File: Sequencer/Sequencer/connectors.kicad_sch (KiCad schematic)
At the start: 1 part, among them J13 Conn_02x05_Odd_Even

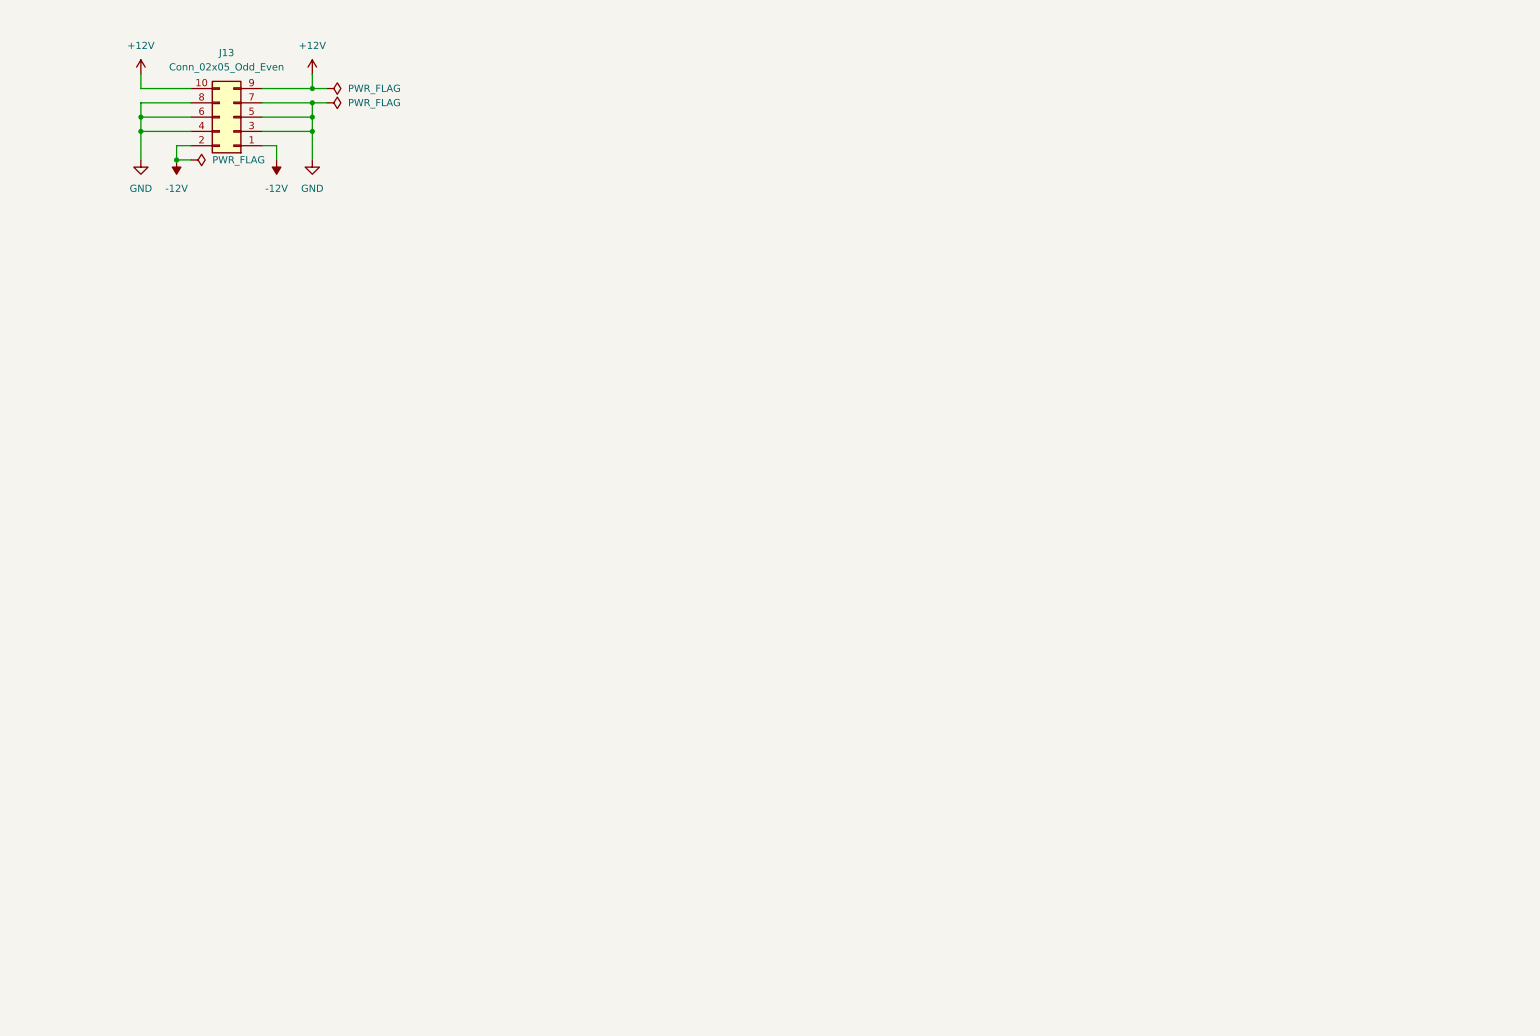
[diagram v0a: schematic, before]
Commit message: Sequencer - schematic mostly complete
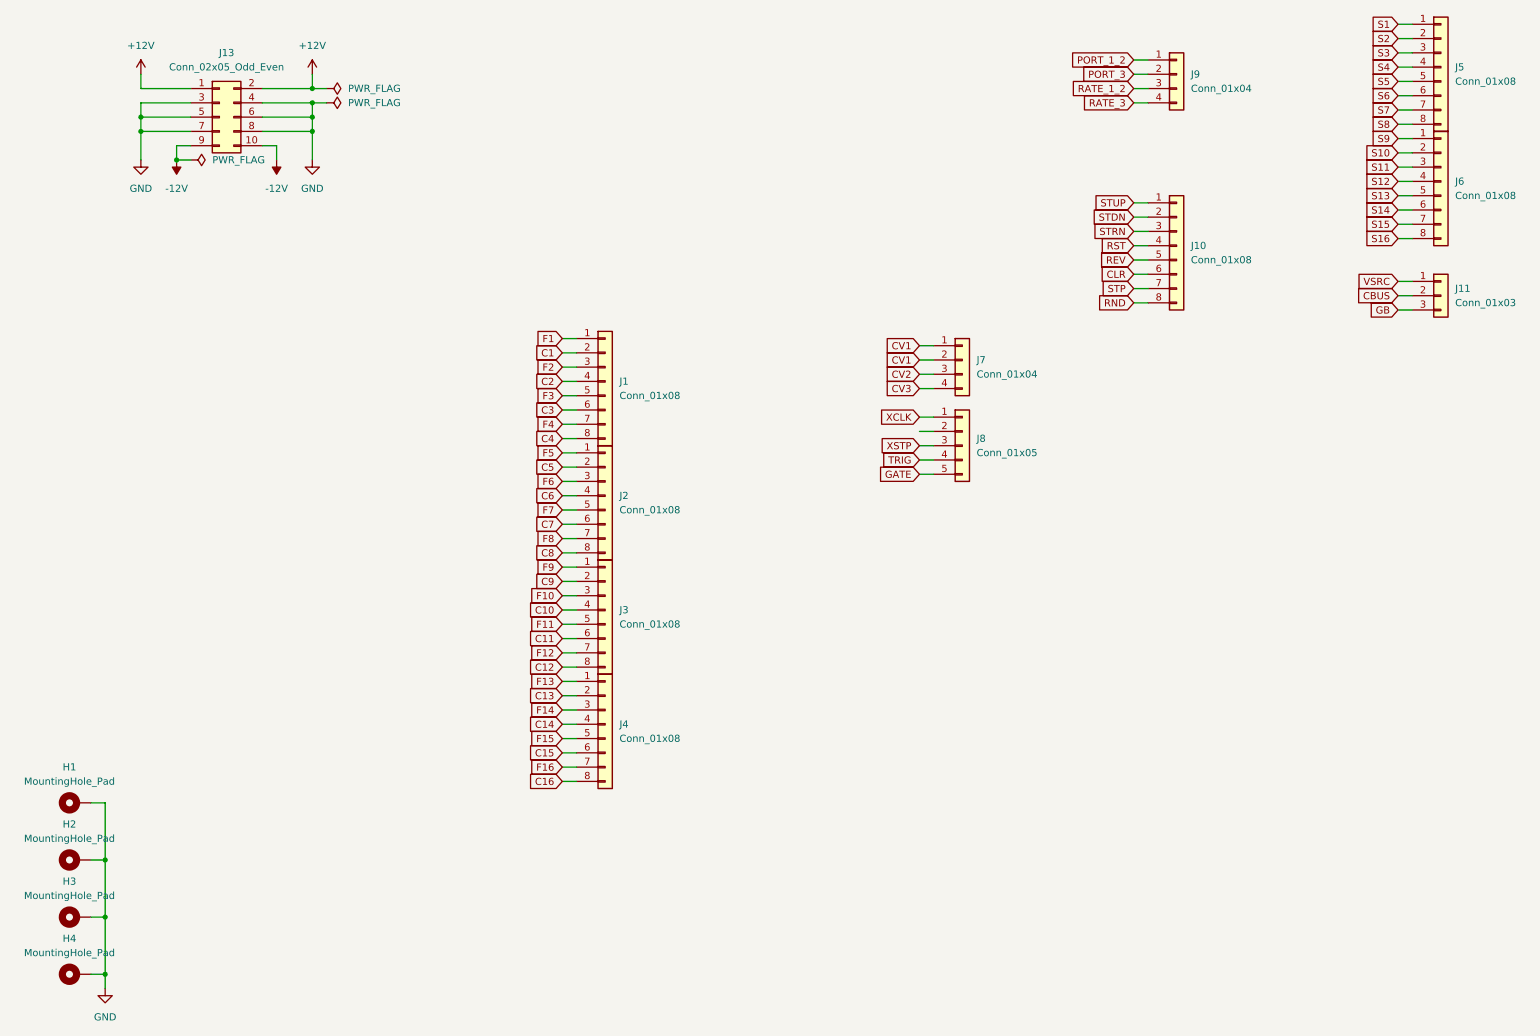
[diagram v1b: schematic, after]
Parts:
- added H1, H2, H3, H4: MountingHole_Pad, MountingHole:MountingHole_3.2mm_M3_Pad, symbol Mechanical:MountingHole_Pad
- added J1, J10, J2, J3, J4, J5, J6: Conn_01x08, Connector_PinHeader_2.54mm:PinHeader_1x08_P2.54mm_Vertical, symbol Connector_Generic:Conn_01x08
- added J11: Conn_01x03, Connector_PinHeader_2.54mm:PinHeader_1x03_P2.54mm_Vertical, symbol Connector_Generic:Conn_01x03
- added J7, J9: Conn_01x04, Connector_PinHeader_2.54mm:PinHeader_1x04_P2.54mm_Vertical, symbol Connector_Generic:Conn_01x04
- added J8: Conn_01x05, Connector_PinHeader_2.54mm:PinHeader_1x05_P2.54mm_Vertical, symbol Connector_Generic:Conn_01x05
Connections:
- net +12V: now also J13.1 (Pin_1), J13.2 (Pin_2); no longer J13.10 (Pin_10), J13.9 (Pin_9)
- net -12V: now also J13.10 (Pin_10), J13.9 (Pin_9); no longer J13.1 (Pin_1), J13.2 (Pin_2)
- net GND: now also H1.1, H2.1, H3.1, H4.1
- new net C1: J1.2 (Pin_2)
- new net C10: J3.4 (Pin_4)
- new net C11: J3.6 (Pin_6)
- new net C12: J3.8 (Pin_8)
- new net C13: J4.2 (Pin_2)
- new net C14: J4.4 (Pin_4)
- new net C15: J4.6 (Pin_6)
- new net C16: J4.8 (Pin_8)
- new net C2: J1.4 (Pin_4)
- new net C3: J1.6 (Pin_6)
- new net C4: J1.8 (Pin_8)
- new net C5: J2.2 (Pin_2)
- new net C6: J2.4 (Pin_4)
- new net C7: J2.6 (Pin_6)
- new net C8: J2.8 (Pin_8)
- new net C9: J3.2 (Pin_2)
- new net CBUS: J11.2 (Pin_2)
- new net CLR: J10.6 (Pin_6)
- new net CV1: J7.1 (Pin_1), J7.2 (Pin_2)
- new net CV2: J7.3 (Pin_3)
- new net CV3: J7.4 (Pin_4)
- new net F1: J1.1 (Pin_1)
- new net F10: J3.3 (Pin_3)
- new net F11: J3.5 (Pin_5)
- new net F12: J3.7 (Pin_7)
- new net F13: J4.1 (Pin_1)
- new net F14: J4.3 (Pin_3)
- new net F15: J4.5 (Pin_5)
- new net F16: J4.7 (Pin_7)
- new net F2: J1.3 (Pin_3)
- new net F3: J1.5 (Pin_5)
- new net F4: J1.7 (Pin_7)
- new net F5: J2.1 (Pin_1)
- new net F6: J2.3 (Pin_3)
- new net F7: J2.5 (Pin_5)
- new net F8: J2.7 (Pin_7)
- new net F9: J3.1 (Pin_1)
- new net GATE: J8.5 (Pin_5)
- new net GB: J11.3 (Pin_3)
- new net PORT_1_2: J9.1 (Pin_1)
- new net PORT_3: J9.2 (Pin_2)
- new net RATE_1_2: J9.3 (Pin_3)
- new net RATE_3: J9.4 (Pin_4)
- new net REV: J10.5 (Pin_5)
- new net RND: J10.8 (Pin_8)
- new net RST: J10.4 (Pin_4)
- new net S1: J5.1 (Pin_1)
- new net S10: J6.2 (Pin_2)
- new net S11: J6.3 (Pin_3)
- new net S12: J6.4 (Pin_4)
- new net S13: J6.5 (Pin_5)
- new net S14: J6.6 (Pin_6)
- new net S15: J6.7 (Pin_7)
- new net S16: J6.8 (Pin_8)
- new net S2: J5.2 (Pin_2)
- new net S3: J5.3 (Pin_3)
- new net S4: J5.4 (Pin_4)
- new net S5: J5.5 (Pin_5)
- new net S6: J5.6 (Pin_6)
- new net S7: J5.7 (Pin_7)
- new net S8: J5.8 (Pin_8)
- new net S9: J6.1 (Pin_1)
- new net STDN: J10.2 (Pin_2)
- new net STP: J10.7 (Pin_7)
- new net STRN: J10.3 (Pin_3)
- new net STUP: J10.1 (Pin_1)
- new net TRIG: J8.4 (Pin_4)
- new net VSRC: J11.1 (Pin_1)
- new net XCLK: J8.1 (Pin_1)
- new net XSTP: J8.3 (Pin_3)
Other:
- moved on the sheet: J13

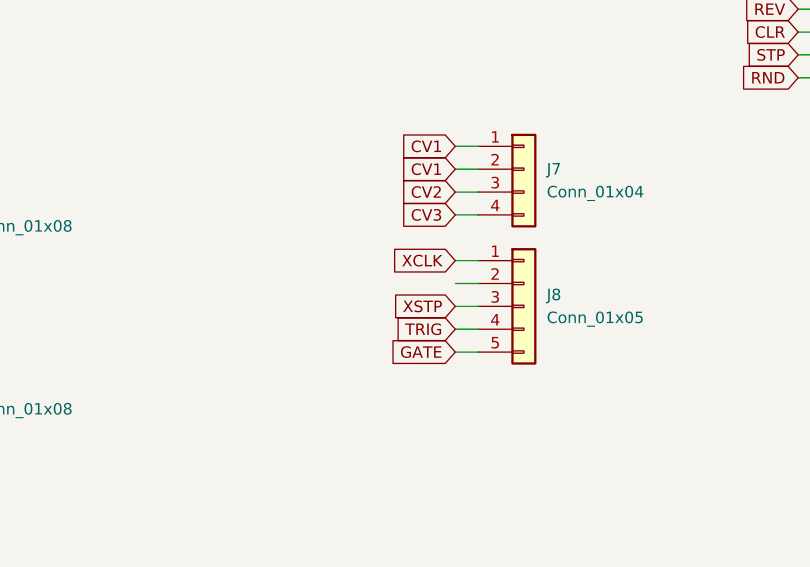
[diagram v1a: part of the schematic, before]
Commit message: Sequencer - minor progress on routing
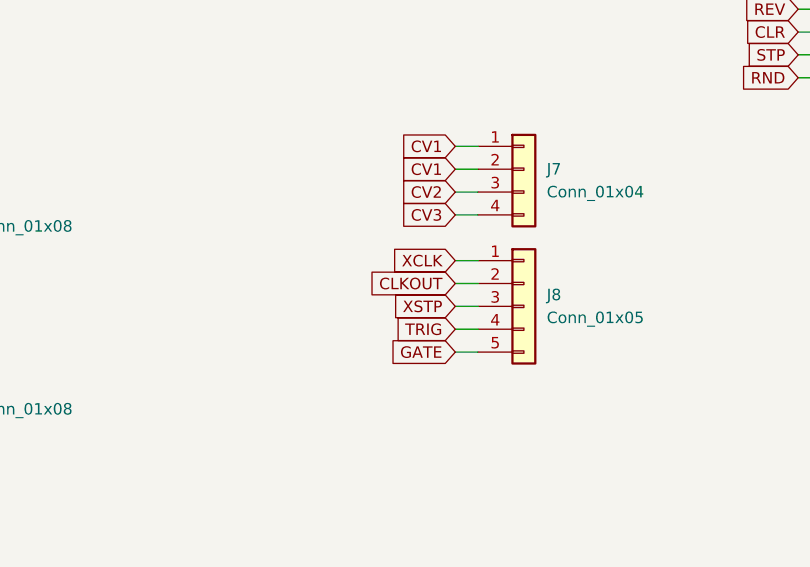
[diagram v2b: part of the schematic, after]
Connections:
- net CLKOUT: now reaches J8.2 (Pin_2)
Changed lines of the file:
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@@
+    )
+  )
+  (global_label "CLKOUT" (shape input) (at 173.99 92.71 180) (fields_autoplaced)
+    (effects (font (size 1.27 1.27)) (justify right))
+    (property "Intersheetrefs" "${INTERSHEET_REFS}" (at 163.8081 92.71 0)
+      (effects (font (size 1.27 1.27)) (justify right) hide)
     )
   )

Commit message: Sequencer - misc
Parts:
- added J7: Conn_01x04, Connector_PinHeader_2.54mm:PinHeader_1x01_P2.54mm_Vertical, symbol Connector_Generic:Conn_01x01
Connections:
- new net RIN: J7.1 (Pin_1)
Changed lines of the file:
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@@
+    (stroke (width 0) (type default))
+  )
+  (polyline (pts (xy 161.29 129.54) (xy 161.29 129.54))
     (stroke (width 0) (type default))
   )
@@
     (stroke (width 0) (type default))
   )
+  (wire (pts (xy 173.99 105.41) (xy 176.53 105.41))
+    (stroke (width 0) (type default))
+  )
   (wire (pts (xy 110.49 81.28) (xy 113.03 81.28))
     (stroke (width 0) (type default))
@@
     (stroke (width 0) (type default))
   )
+  (polyline (pts (xy 161.29 129.54) (xy 161.29 129.54))
+    (stroke (width 0) (type default))
+  )
   (wire (pts (xy 212.09 26.67) (xy 214.63 26.67))
     (stroke (width 0) (type default))
@@
     (effects (font (size 1.27 1.27)) (justify right))
     (property "Intersheetrefs" "${INTERSHEET_REFS}" (at 105.2067 106.68 0)
+      (effects (font (size 1.27 1.27)) (justify right) hide)
+    )
+  )
+  (global_label "RIN" (shape input) (at 173.99 105.41 180) (fields_autoplaced)
+    (effects (font (size 1.27 1.27)) (justify right))
+    (property "Intersheetrefs" "${INTERSHEET_REFS}" (at 167.7995 105.41 0)
       (effects (font (size 1.27 1.27)) (justify right) hide)
     )
@@
         )
       )
+    )
+  )
+  (symbol (lib_id "Connector_Generic:Conn_01x01") (at 181.61 105.41 0) (unit 1)
+    (in_bom yes) (on_board yes) (dnp no) (fields_autoplaced)
+    (property "Reference" "J7" (at 184.15 104.14 0)
+      (effects (font (size 1.27 1.27)) (justify left))
+    )
+    (property "Value" "Conn_01x04" (at 184.15 106.68 0)
+      (effects (font (size 1.27 1.27)) (justify left))
+    )
+    (property "Footprint" "Connector_PinHeader_2.54mm:PinHeader_1x01_P2.54mm_Vertical" (at 181.61 105.41 0)
+      (effects (font (size 1.27 1.27)) hide)
+    )
+    (property "Datasheet" "~" (at 181.61 105.41 0)
+      (effects (font (size 1.27 1.27)) hide)
+    )
+    (pin "1")
+    (instances
+      (project "Sequencer-controls"
+        (path "/0fe7de3d-0e02-4720-a37d-4e739d042412/aa9fd4ea-0392-4968-bc04-e545f42a920f"
+          (reference "J7") (unit 1)
+        )
+      )
+      (project "Sequencer"
+        (path "/8a8c4421-b74b-4a68-822a-0aad66407659/92ad5e63-2ca1-4c30-8d76-326b48f118bb"
+          (reference "J13") (unit 1)
+        )
+      )
